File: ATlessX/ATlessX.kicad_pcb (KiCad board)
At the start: 2 copper layers, 0 parts

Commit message: Update PCB schematic
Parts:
- added C1: 1uF, Capacitor_THT:CP_Radial_D6.3mm_P2.50mm, F.Cu at (73.2, 74.4)
- added C2: 10uF, Capacitor_THT:CP_Radial_D6.3mm_P2.50mm, F.Cu at (87.9, 72.6)
- added D1: 1N4148, Diode_THT:D_DO-35_SOD27_P7.62mm_Horizontal, F.Cu at (75.8, 82.6)
- added D2: 1N4148, Diode_THT:D_DO-35_SOD27_P7.62mm_Horizontal, F.Cu at (48.0, 98.6)
- added D3: 5VSB, LED_THT:LED_D3.0mm, F.Cu at (141.2, 32.5)
- added D4: +5V, LED_THT:LED_D3.0mm, F.Cu at (141.2, 37.1)
- added D5: +12V, LED_THT:LED_D3.0mm, F.Cu at (141.2, 41.7)
- added D6: -12V, LED_THT:LED_D3.0mm, F.Cu at (138.7, 46.2)
- added D7: -5V, LED_THT:LED_D3.0mm, F.Cu at (138.7, 50.8)
- added J1: EXT_PWR_SW, Connector_PinHeader_2.54mm:PinHeader_1x02_P2.54mm_Vertical, F.Cu at (102.1, 72.6)
- added J2: ATX, Connector_Molex:Molex_Mini-Fit_Jr_5566-20A_2x10_P4.20mm_Vertical, F.Cu at (85.6, 24.6)
- added J3: P8, Connector_Molex:Molex_KK-254_AE-6410-06A_1x06_P2.54mm_Vertical, F.Cu at (69.8, 95.8)
- added J4: P9, Connector_Molex:Molex_KK-254_AE-6410-06A_1x06_P2.54mm_Vertical, F.Cu at (91.7, 96.8)
- added R1: 10K, Resistor_THT:R_Axial_DIN0207_L6.3mm_D2.5mm_P10.16mm_Horizontal, F.Cu at (51.3, 81.0)
- added R2: 10K, Resistor_THT:R_Axial_DIN0207_L6.3mm_D2.5mm_P10.16mm_Horizontal, F.Cu at (86.3, 82.0)
- added R3: 470, Resistor_THT:R_Axial_DIN0207_L6.3mm_D2.5mm_P10.16mm_Horizontal, F.Cu at (44.2, 68.1)
- added RN1: 10K, Resistor_THT:R_Array_SIP6, F.Cu at (150.4, 33.5)
- added SW1: Power, Button_Switch_THT:SW_PUSH_6mm, F.Cu at (58.9, 71.9)
- added U1: 74LS74, Package_DIP:DIP-14_W7.62mm_Socket_LongPads, F.Cu at (93.2, 46.5)
- added U2: 74LS14, Package_DIP:DIP-14_W7.62mm_Socket_LongPads, F.Cu at (80.0, 46.5)
- added U3: L7905, Package_TO_SOT_THT:TO-220-3_Horizontal_TabDown, F.Cu at (66.5, 47.2)
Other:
- net class Default: trace_width 0.25 -> 0.3
- net class High_Power added: clearance 0.4, trace_width 1.5, via_dia 1, via_drill 0.4
- net class Low_Power added: clearance 0.2, trace_width 0.6, via_dia 1, via_drill 0.4

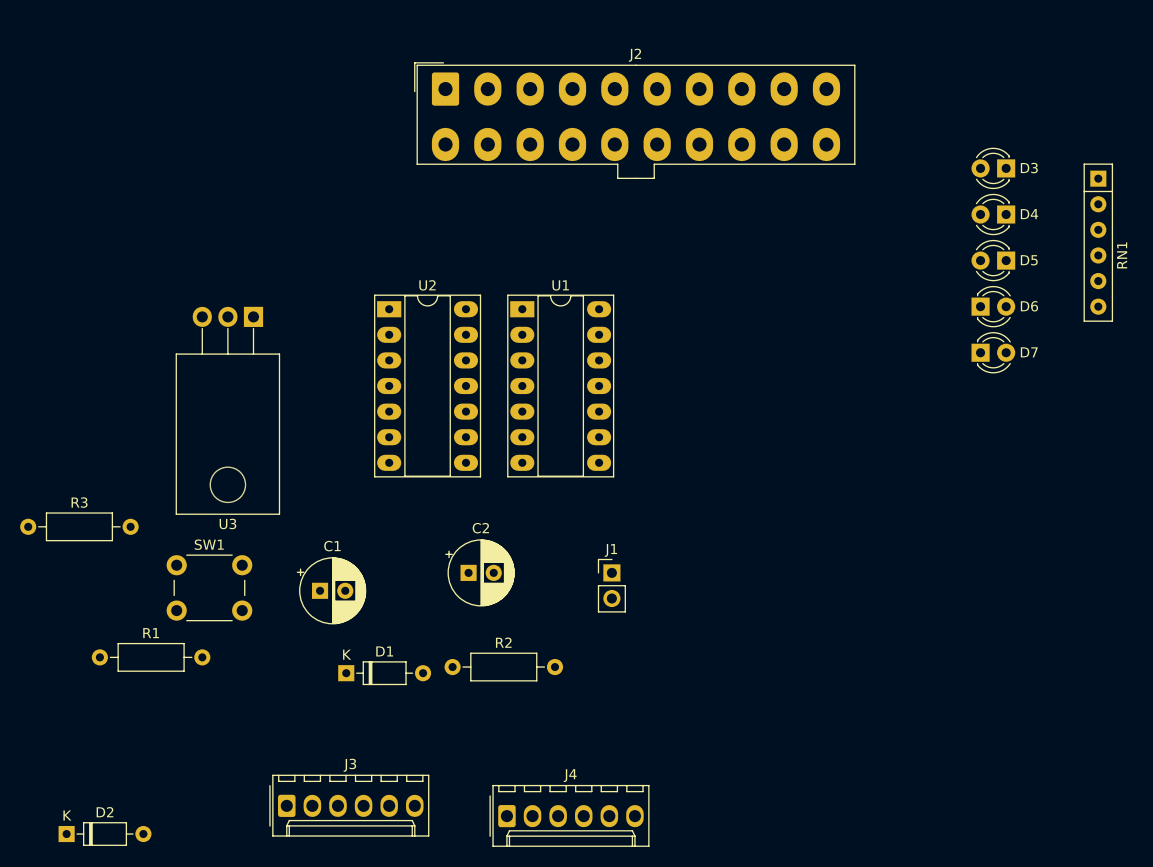
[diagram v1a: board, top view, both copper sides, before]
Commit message: Add filter caps
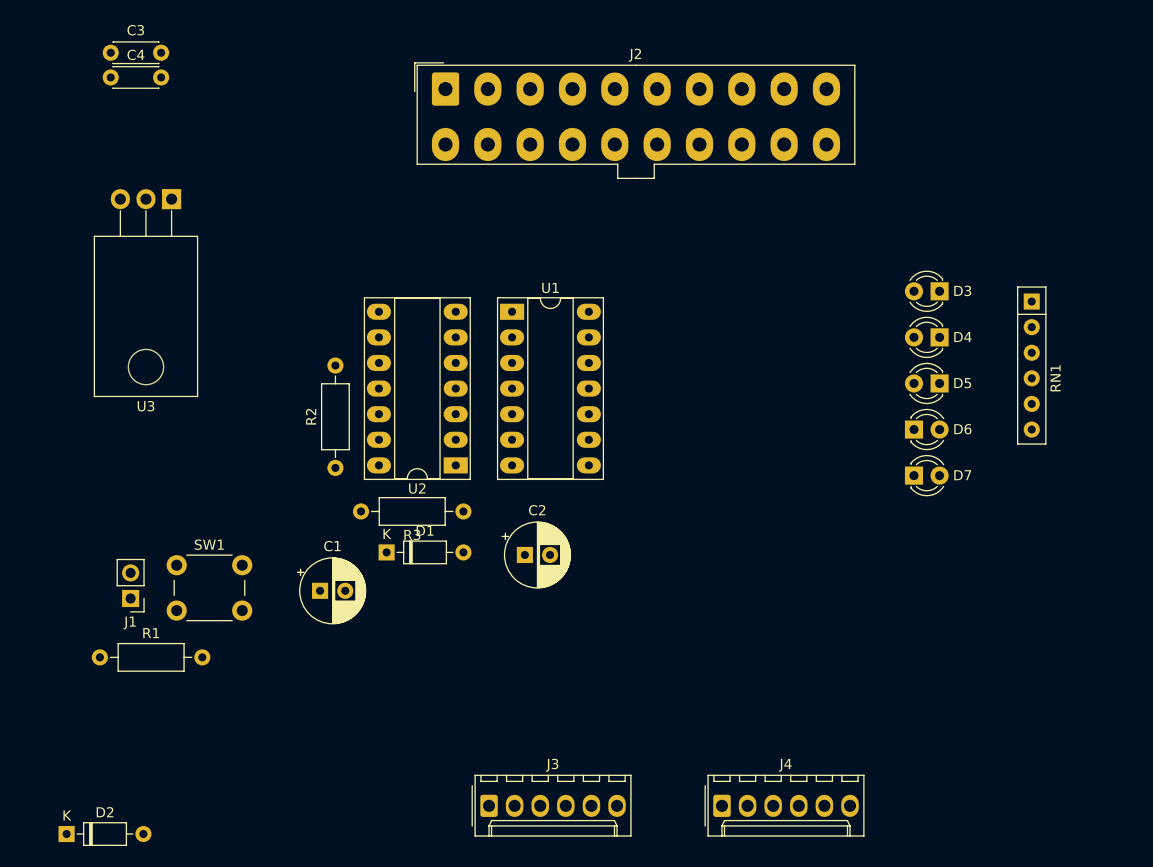
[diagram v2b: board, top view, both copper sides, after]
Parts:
- added C3: 100nF, Capacitor_THT:C_Disc_D4.3mm_W1.9mm_P5.00mm, F.Cu at (52.4, 21.0)
- added C4: 100nF, Capacitor_THT:C_Disc_D4.3mm_W1.9mm_P5.00mm, F.Cu at (52.4, 23.5)
- moved J1 47.8 mm to (54.4, 75.2), turned to 180 degrees
- moved R3 43.2 mm to (87.4, 66.5), turned to 180 degrees
- moved R2 22.9 mm to (74.7, 62.2), turned to 90 degrees
- moved J4 21.4 mm to (113.0, 95.8)
- moved J3 20.1 mm to (89.9, 95.8)
- moved U2 16.8 mm to (86.6, 62.0), turned to 180 degrees
- moved U3 14.2 mm to (58.4, 35.6)
- moved D3 13.9 mm to (134.6, 44.7)
- moved D4 13.9 mm to (134.6, 49.3)
- moved D5 13.9 mm to (134.6, 53.8)
- moved D6 13.9 mm to (132.1, 58.4)
- moved D7 13.9 mm to (132.1, 63.0)
- moved RN1 13.9 mm to (143.8, 45.7)
- moved D1 12.6 mm to (79.8, 70.6)
- moved C2 5.86 mm to (93.5, 70.9)
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
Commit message: Some more work
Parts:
- moved D2 51.5 mm to (87.9, 66.0), turned to 270 degrees
- moved C3 46.7 mm to (93.2, 43.7)
- moved C4 35.0 mm to (81.0, 43.7)
- moved R1 31.0 mm to (78.5, 66.0), turned to 180 degrees
- moved C1 24.5 mm to (97.5, 77.0), turned to 270 degrees
- moved R3 21.4 mm to (71.6, 52.1), turned to 270 degrees
- moved SW1 20.8 mm to (79.5, 74.7), turned to 180 degrees
- moved U2 16.6 mm to (80.0, 46.7), turned to 0 degrees
- moved J1 15.4 mm to (69.1, 70.9), turned to 0 degrees
- moved U3 13.6 mm to (70.6, 41.7), turned to 0 degrees
- moved D3 11.7 mm to (123.2, 47.2)
- moved D4 11.7 mm to (123.2, 51.8)
- moved D5 11.7 mm to (123.2, 56.4)
- moved D6 11.7 mm to (120.7, 61.0)
- moved D7 11.7 mm to (120.7, 65.5)
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
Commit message: Design PCB
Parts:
- added H1: MountingHole_Pad, MountingHole:MountingHole_3.5mm_Pad, F.Cu at (139.7, 27.9)
- added H2: MountingHole_Pad, MountingHole:MountingHole_3.5mm_Pad, F.Cu at (59.7, 27.9)
- added H3: MountingHole_Pad, MountingHole:MountingHole_3.5mm_Pad, F.Cu at (139.7, 87.6)
- added H4: MountingHole_Pad, MountingHole:MountingHole_3.5mm_Pad, F.Cu at (59.7, 87.6)
- moved C2 40.3 mm to (62.2, 64.8), turned to 180 degrees
- moved R1 35.4 mm to (58.4, 36.8), turned to 270 degrees
- moved C1 35.4 mm to (62.2, 74.9), turned to 180 degrees
- moved U2 24.7 mm to (68.6, 68.6)
- moved U1 23.9 mm to (82.5, 68.6)
- moved C4 22.7 mm to (69.8, 63.5)
- moved J1 22.7 mm to (58.4, 50.8)
- moved C3 21.9 mm to (83.8, 63.5)
- moved SW1 20.6 mm to (71.1, 55.9)
- moved R3 18.3 mm to (61.5, 36.8)
- moved R2 18.3 mm to (64.5, 47.0)
- moved D7 13.9 mm to (133.3, 71.1)
- moved D6 13.7 mm to (133.3, 66.0)
- moved D5 13.5 mm to (135.9, 61.0)
- moved D4 13.3 mm to (135.9, 55.9)
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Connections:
- U1 pad 10: (no net) -> /5VSB
- U1 pad 11: (no net) -> GND
- U1 pad 12: (no net) -> GND
- U1 pad 13: (no net) -> GND
- U1 pad 8: (no net) -> Net-(U1-Pad8)
- U1 pad 9: (no net) -> Net-(U1-Pad9)
- U2 pad 10: (no net) -> Net-(U2-Pad10)
- U2 pad 11: (no net) -> GND
- U2 pad 12: (no net) -> Net-(U2-Pad12)
- U2 pad 13: (no net) -> GND
- U2 pad 8: (no net) -> Net-(U2-Pad8)
- U2 pad 9: (no net) -> GND
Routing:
- net GND: track 0.00 -> 433.5 mm
- net /5VSB: track 0.00 -> 188.9 mm
- net VCC: track 0.00 -> 187.7 mm
- net /-12V: track 0.00 -> 113.3 mm
- net /+12V: track 0.00 -> 90.8 mm, vias 0 -> 3
- net /-5V: track 0.00 -> 83.3 mm, vias 0 -> 1
- net /PWR_OK: track 0.00 -> 72.2 mm, vias 0 -> 1
- net /~PS_ON: track 0.00 -> 59.0 mm
- net Net-(C2-Pad1): track 0.00 -> 52.1 mm, vias 0 -> 1
- net Net-(C1-Pad1): track 0.00 -> 50.7 mm
- net /PWR_SW: track 0.00 -> 19.1 mm
- net Net-(U1-Pad4): track 0.00 -> 16.1 mm
- net Net-(U1-Pad3): track 0.00 -> 15.7 mm
- net Net-(U1-Pad2): track 0.00 -> 13.2 mm
- net Net-(D3-Pad1): track 0.00 -> 6.66 mm
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- added copper zone on B.Cu, net /+12V
- added copper zone on F.Cu, net /+12V
- added copper zone on F.Cu, net /-12V
- added copper zone on F.Cu, net /-5V
- added copper zone on B.Cu, net GND
- added copper zone on F.Cu, net GND
- added copper zone on In2.Cu, net GND
- added copper zone on In1.Cu, net VCC
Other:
- board outline added: 90.2 x 73.7 mm
- copper layers 2 -> 4
- net class Low_Power: trace_width 0.6 -> 1
